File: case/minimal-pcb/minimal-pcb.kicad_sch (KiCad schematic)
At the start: 10 parts, among them J1 USB_C_Receptacle_USB2.0

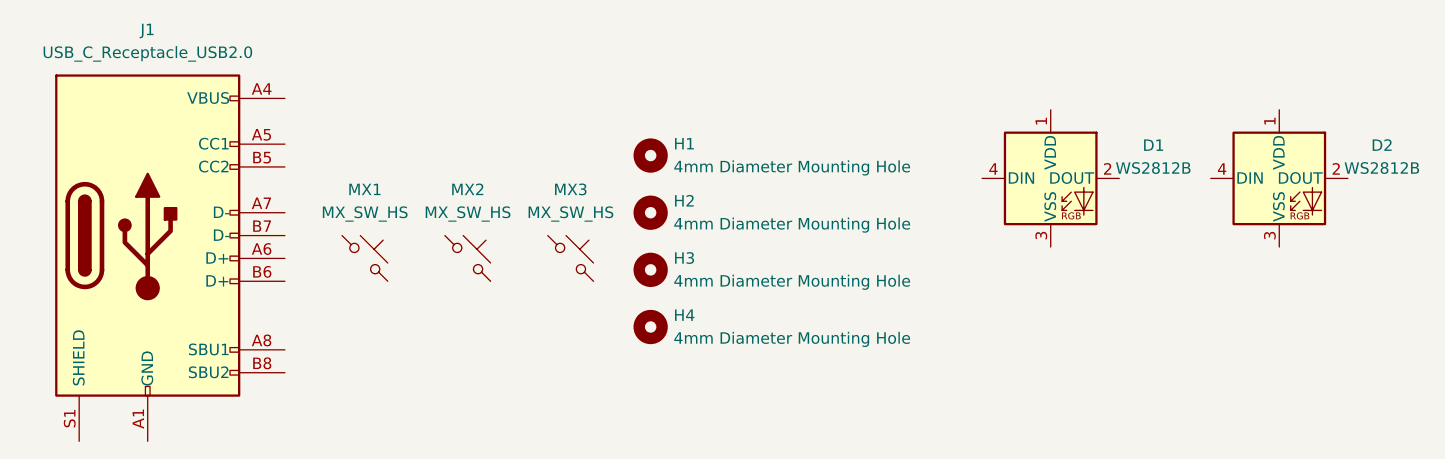
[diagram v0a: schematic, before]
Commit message: fix: use padded 3.5mm mounting holes in minimal PCB
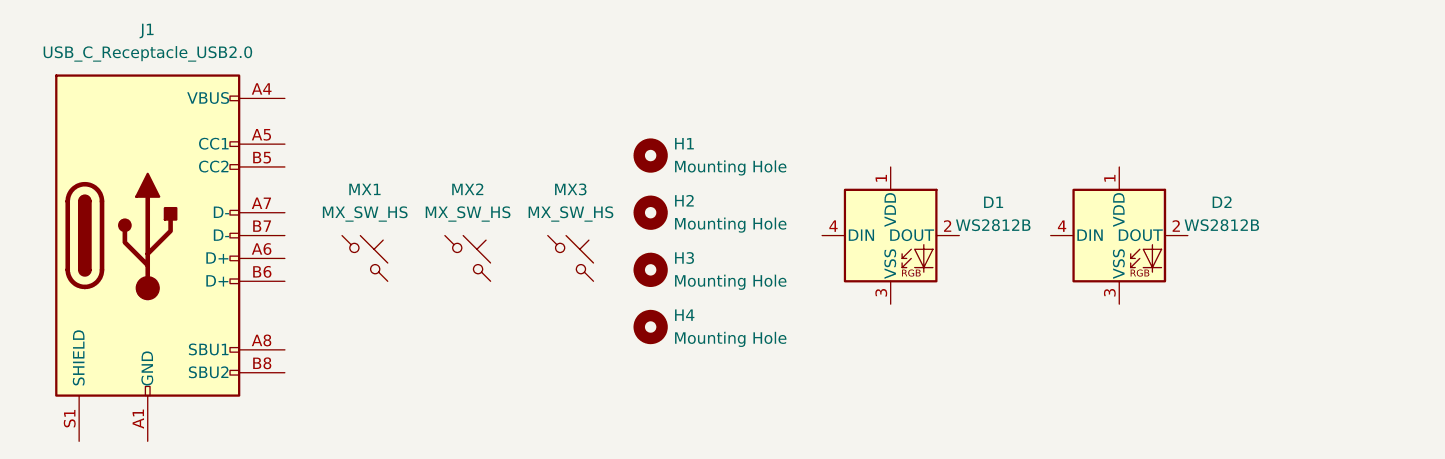
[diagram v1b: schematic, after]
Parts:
- H1, H2, H3, H4: value 4mm Diameter Mounting Hole -> Mounting Hole; footprint MountingHole:MountingHole_4mm -> MountingHole:MountingHole_3.5mm_Pad
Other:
- moved on the sheet: D1, D2
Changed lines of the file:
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@@
 (kicad_sch (version 20230121) (generator eeschema)
   (paper "A4")
-  (symbol (lib_id "LED:WS2812B") (at 152.4 31.75 0) (unit 1)
-    (in_bom yes) (on_board yes) (dnp no) (fields_autoplaced)
-    (property "Reference" "D2" (at 163.83 28.1021 0)
-      (effects (font (size 1.27 1.27)))
-    )
-    (property "Value" "WS2812B" (at 163.83 30.6421 0)
-      (effects (font (size 1.27 1.27)))
-    )
-    (property "Footprint" "LED_SMD:LED_WS2812B_PLCC4_5.0x5.0mm_P3.2mm" (at 153.67 39.37 0)
-      (effects (font (size 1.27 1.27)) (justify left top) hide)
-    )
-    (property "Datasheet" "https://cdn-shop.adafruit.com/datasheets/WS2812B.pdf" (at 154.94 41.275 0)
+  (symbol (lib_id "LED:WS2812B") (at 134.62 38.1 0) (unit 1)
+    (in_bom yes) (on_board yes) (dnp no) (fields_autoplaced)
+    (property "Reference" "D2" (at 146.05 34.4521 0)
+      (effects (font (size 1.27 1.27)))
+    )
+    (property "Value" "WS2812B" (at 146.05 36.9921 0)
+      (effects (font (size 1.27 1.27)))
+    )
+    (property "Footprint" "LED_SMD:LED_WS2812B_PLCC4_5.0x5.0mm_P3.2mm" (at 135.89 45.72 0)
+      (effects (font (size 1.27 1.27)) (justify left top) hide)
+    )
+    (property "Datasheet" "https://cdn-shop.adafruit.com/datasheets/WS2812B.pdf" (at 137.16 47.625 0)
       (effects (font (size 1.27 1.27)) (justify left top) hide)
     )
@@
     )
   )
-  (symbol (lib_id "LED:WS2812B") (at 127 31.75 0) (unit 1)
-    (in_bom yes) (on_board yes) (dnp no) (fields_autoplaced)
-    (property "Reference" "D1" (at 138.43 28.1021 0)
-      (effects (font (size 1.27 1.27)))
-    )
-    (property "Value" "WS2812B" (at 138.43 30.6421 0)
-      (effects (font (size 1.27 1.27)))
-    )
-    (property "Footprint" "LED_SMD:LED_WS2812B_PLCC4_5.0x5.0mm_P3.2mm" (at 128.27 39.37 0)
-      (effects (font (size 1.27 1.27)) (justify left top) hide)
-    )
-    (property "Datasheet" "https://cdn-shop.adafruit.com/datasheets/WS2812B.pdf" (at 129.54 41.275 0)
+  (symbol (lib_id "LED:WS2812B") (at 109.22 38.1 0) (unit 1)
+    (in_bom yes) (on_board yes) (dnp no) (fields_autoplaced)
+    (property "Reference" "D1" (at 120.65 34.4521 0)
+      (effects (font (size 1.27 1.27)))
+    )
+    (property "Value" "WS2812B" (at 120.65 36.9921 0)
+      (effects (font (size 1.27 1.27)))
+    )
+    (property "Footprint" "LED_SMD:LED_WS2812B_PLCC4_5.0x5.0mm_P3.2mm" (at 110.49 45.72 0)
+      (effects (font (size 1.27 1.27)) (justify left top) hide)
+    )
+    (property "Datasheet" "https://cdn-shop.adafruit.com/datasheets/WS2812B.pdf" (at 111.76 47.625 0)
       (effects (font (size 1.27 1.27)) (justify left top) hide)
     )
@@
       (effects (font (size 1.27 1.27)) (justify left))
     )
-    (property "Value" "4mm Diameter Mounting Hole" (at 85.09 49.53 0)
-      (effects (font (size 1.27 1.27)) (justify left))
-    )
-    (property "Footprint" "MountingHole:MountingHole_4mm" (at 82.55 48.26 0)
+    (property "Value" "Mounting Hole" (at 85.09 49.53 0)
+      (effects (font (size 1.27 1.27)) (justify left))
+    )
+    (property "Footprint" "MountingHole:MountingHole_3.5mm_Pad" (at 82.55 48.26 0)
       (effects (font (size 1.27 1.27)) hide)
     )
@@
       (effects (font (size 1.27 1.27)) (justify left))
     )
-    (property "Value" "4mm Diameter Mounting Hole" (at 85.09 43.18 0)
-      (effects (font (size 1.27 1.27)) (justify left))
-    )
-    (property "Footprint" "MountingHole:MountingHole_4mm" (at 82.55 41.91 0)
+    (property "Value" "Mounting Hole" (at 85.09 43.18 0)
+      (effects (font (size 1.27 1.27)) (justify left))
+    )
+    (property "Footprint" "MountingHole:MountingHole_3.5mm_Pad" (at 82.55 41.91 0)
       (effects (font (size 1.27 1.27)) hide)
     )
@@
       (effects (font (size 1.27 1.27)) (justify left))
     )
-    (property "Value" "4mm Diameter Mounting Hole" (at 85.09 30.48 0)
-      (effects (font (size 1.27 1.27)) (justify left))
-    )
-    (property "Footprint" "MountingHole:MountingHole_4mm" (at 82.55 29.21 0)
+    (property "Value" "Mounting Hole" (at 85.09 30.48 0)
+      (effects (font (size 1.27 1.27)) (justify left))
+    )
+    (property "Footprint" "MountingHole:MountingHole_3.5mm_Pad" (at 82.55 29.21 0)
       (effects (font (size 1.27 1.27)) hide)
     )
@@
       (effects (font (size 1.27 1.27)) (justify left))
     )
-    (property "Value" "4mm Diameter Mounting Hole" (at 85.09 36.83 0)
-      (effects (font (size 1.27 1.27)) (justify left))
-    )
-    (property "Footprint" "MountingHole:MountingHole_4mm" (at 82.55 35.56 0)
-      (effects (font (size 1.27 1.27)) hide)
-    )
+    (property "Value" "Mounting Hole" (at 85.09 36.83 0)
+      (effects (font (size 1.27 1.27)) (justify left))
+    )
+    (property "Footprint" "MountingHole:MountingHole_3.5mm_Pad" (at 82.55 35.56 0)
+      (effects (font (size 1.27 1.27)) hide)
+    )

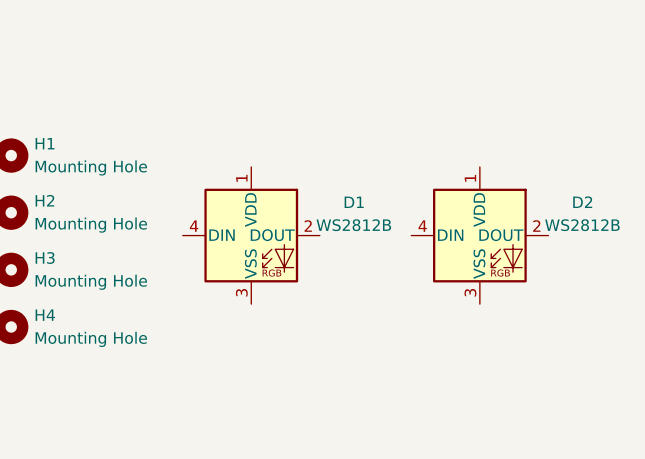
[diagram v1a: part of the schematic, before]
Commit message: chore: update minimal pcb
got the usb cutout dimensions wrong on the pcb... need to fix it
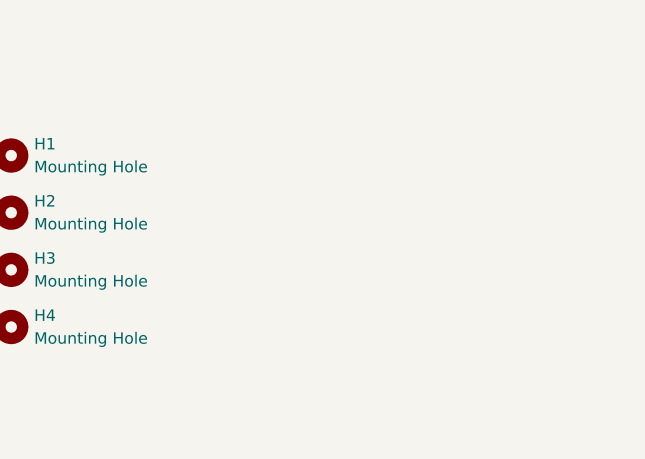
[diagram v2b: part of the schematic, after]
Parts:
- removed D1, D2: WS2812B, LED_SMD:LED_WS2812B_PLCC4_5.0x5.0mm_P3.2mm, symbol LED:WS2812B
- H1, H2, H3, H4: footprint MountingHole:MountingHole_3.5mm_Pad -> MountingHole:MountingHole_2.2mm_M2_Pad
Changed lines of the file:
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@@
 (kicad_sch (version 20230121) (generator eeschema)
   (paper "A4")
-  (symbol (lib_id "LED:WS2812B") (at 134.62 38.1 0) (unit 1)
-    (in_bom yes) (on_board yes) (dnp no) (fields_autoplaced)
-    (property "Reference" "D2" (at 146.05 34.4521 0)
-      (effects (font (size 1.27 1.27)))
-    )
-    (property "Value" "WS2812B" (at 146.05 36.9921 0)
-      (effects (font (size 1.27 1.27)))
-    )
-    (property "Footprint" "LED_SMD:LED_WS2812B_PLCC4_5.0x5.0mm_P3.2mm" (at 135.89 45.72 0)
-      (effects (font (size 1.27 1.27)) (justify left top) hide)
-    )
-    (property "Datasheet" "https://cdn-shop.adafruit.com/datasheets/WS2812B.pdf" (at 137.16 47.625 0)
-      (effects (font (size 1.27 1.27)) (justify left top) hide)
-    )
-    (pin "3")
-    (pin "2")
-    (pin "1")
-    (pin "4")
-    (instances
-      (project "minimal-pcb"
-        (path "/c344c5d0-cf23-4544-bea1-4c916eeaf203"
-          (reference "D2") (unit 1)
-        )
-      )
-    )
-  )
-  (symbol (lib_id "LED:WS2812B") (at 109.22 38.1 0) (unit 1)
-    (in_bom yes) (on_board yes) (dnp no) (fields_autoplaced)
-    (property "Reference" "D1" (at 120.65 34.4521 0)
-      (effects (font (size 1.27 1.27)))
-    )
-    (property "Value" "WS2812B" (at 120.65 36.9921 0)
-      (effects (font (size 1.27 1.27)))
-    )
-    (property "Footprint" "LED_SMD:LED_WS2812B_PLCC4_5.0x5.0mm_P3.2mm" (at 110.49 45.72 0)
-      (effects (font (size 1.27 1.27)) (justify left top) hide)
-    )
-    (property "Datasheet" "https://cdn-shop.adafruit.com/datasheets/WS2812B.pdf" (at 111.76 47.625 0)
-      (effects (font (size 1.27 1.27)) (justify left top) hide)
-    )
-    (pin "3")
-    (pin "2")
-    (pin "1")
-    (pin "4")
-    (instances
-      (project "minimal-pcb"
-        (path "/c344c5d0-cf23-4544-bea1-4c916eeaf203"
-          (reference "D1") (unit 1)
-        )
-      )
-    )
-  )
   (symbol (lib_id "PCM_marbastlib-mx:MX_SW_HS") (at 50.8 40.64 0) (unit 1)
     (in_bom yes) (on_board yes) (dnp no) (fields_autoplaced)
@@
       (effects (font (size 1.27 1.27)) (justify left))
     )
-    (property "Footprint" "MountingHole:MountingHole_3.5mm_Pad" (at 82.55 48.26 0)
+    (property "Footprint" "MountingHole:MountingHole_2.2mm_M2_Pad" (at 82.55 48.26 0)
       (effects (font (size 1.27 1.27)) hide)
     )
@@
       (effects (font (size 1.27 1.27)) (justify left))
     )
-    (property "Footprint" "MountingHole:MountingHole_3.5mm_Pad" (at 82.55 41.91 0)
+    (property "Footprint" "MountingHole:MountingHole_2.2mm_M2_Pad" (at 82.55 41.91 0)
       (effects (font (size 1.27 1.27)) hide)
     )
@@
       (effects (font (size 1.27 1.27)) (justify left))
     )
-    (property "Footprint" "MountingHole:MountingHole_3.5mm_Pad" (at 82.55 29.21 0)
+    (property "Footprint" "MountingHole:MountingHole_2.2mm_M2_Pad" (at 82.55 29.21 0)
       (effects (font (size 1.27 1.27)) hide)
     )
@@
       (effects (font (size 1.27 1.27)) (justify left))
     )
-    (property "Footprint" "MountingHole:MountingHole_3.5mm_Pad" (at 82.55 35.56 0)
+    (property "Footprint" "MountingHole:MountingHole_2.2mm_M2_Pad" (at 82.55 35.56 0)
       (effects (font (size 1.27 1.27)) hide)
     )
